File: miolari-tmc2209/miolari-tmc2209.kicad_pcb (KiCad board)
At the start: 2 copper layers, 50 x 49 mm, 32 parts, among them J1 Spread, J2 MS1, J3 MS2, J4 TMC2209_Conn, J5 DriverConn, J9 TMC2209_VIN, U2 TMC2209-LA

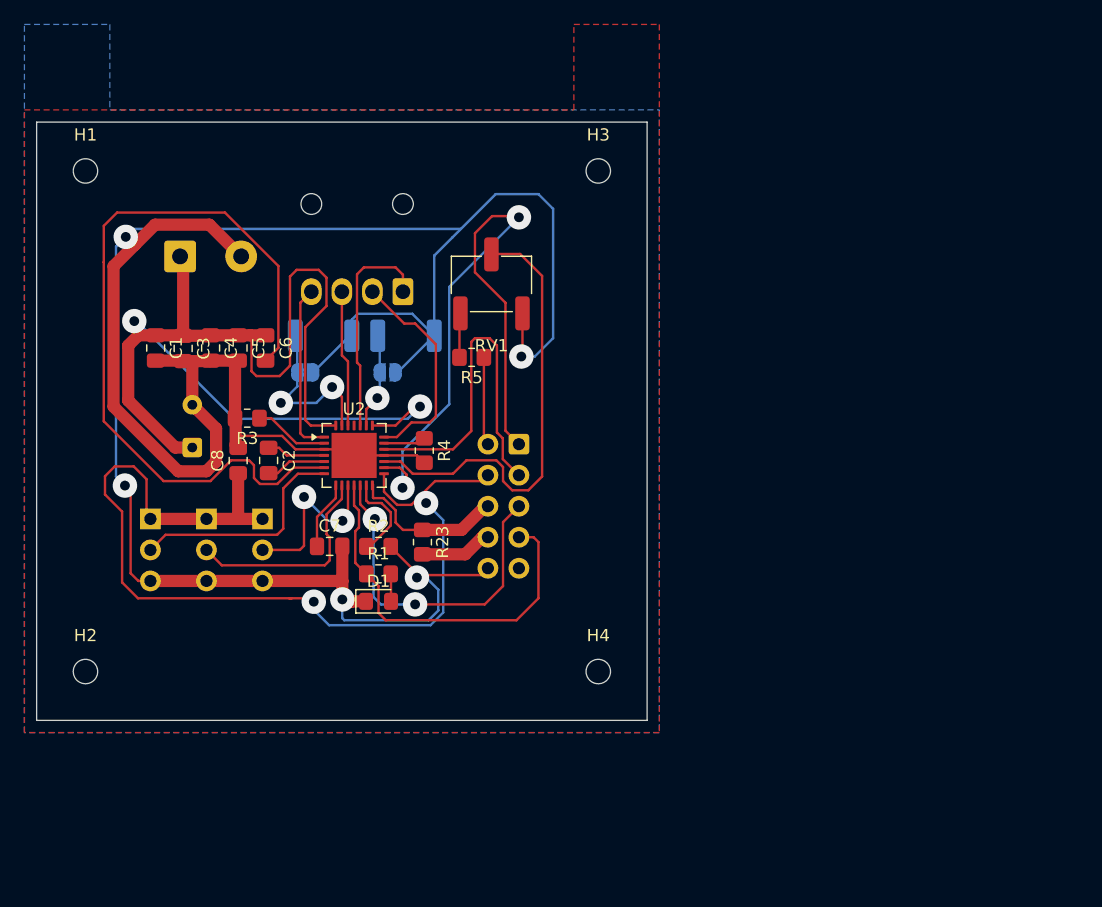
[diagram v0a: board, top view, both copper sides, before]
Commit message: add idc connector to miolari tmc2209
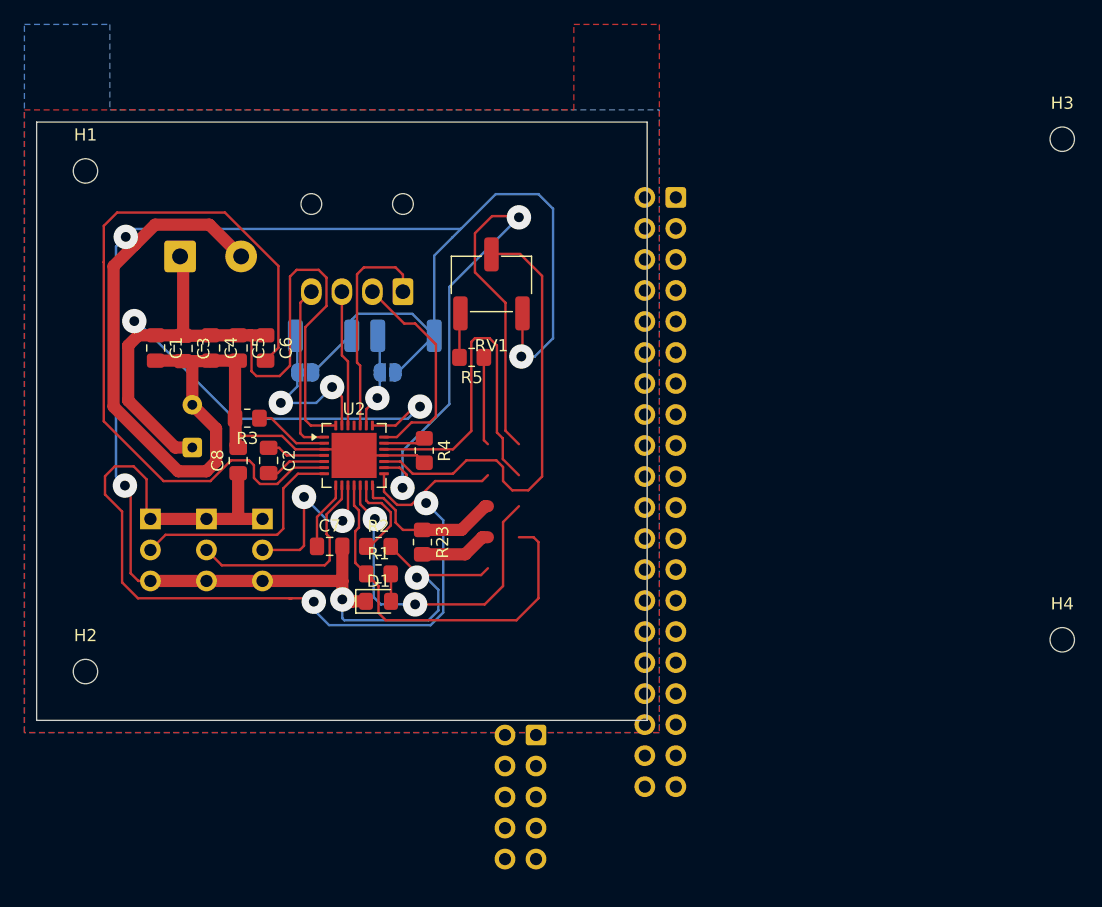
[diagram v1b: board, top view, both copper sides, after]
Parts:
- added J10: MainConnector, Connector_IDC:IDC-Header_2x20_P2.54mm_Vertical, B.Cu at (149.4, 64.2)
- moved H3 38.1 mm to (181.0, 59.4)
- moved H4 38.1 mm to (181.0, 100.4)
- moved J5 23.9 mm to (137.9, 108.2)

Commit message: finish un-tidy miolari tmc2209
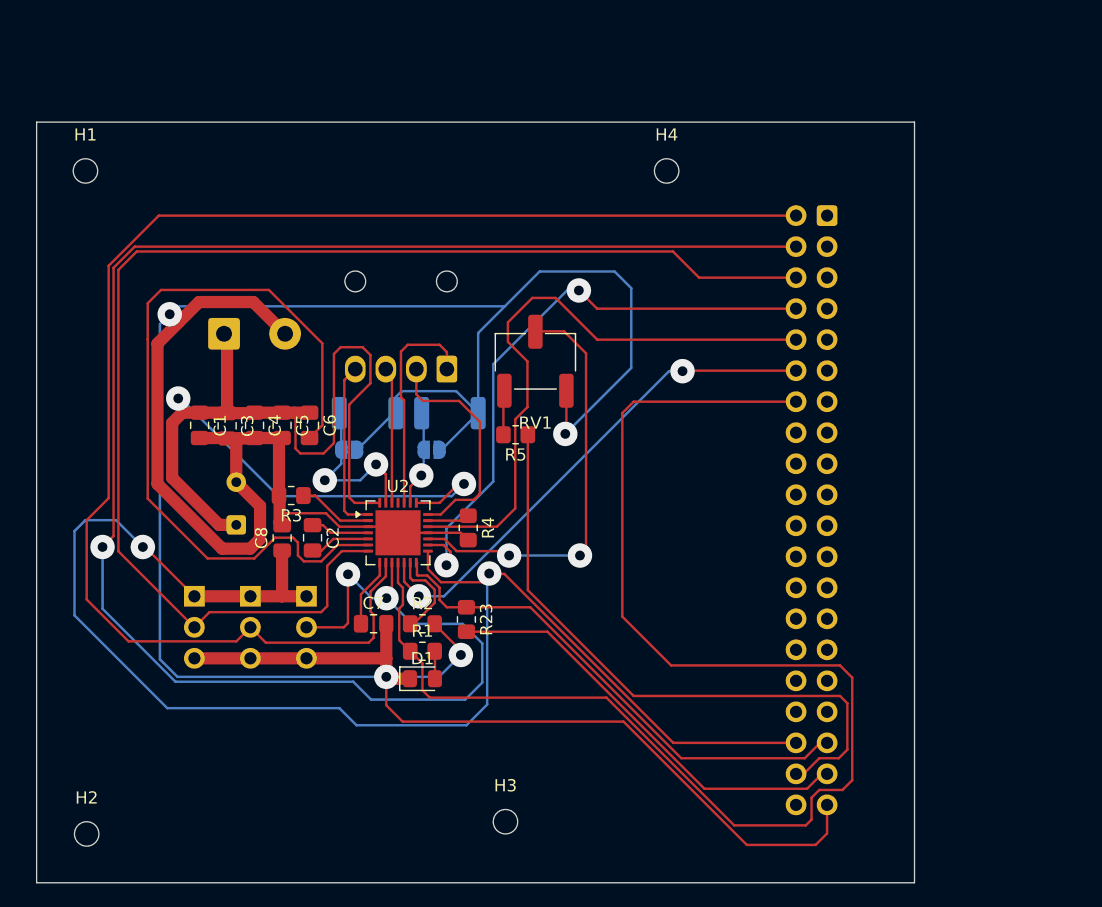
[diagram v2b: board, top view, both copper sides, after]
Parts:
- removed J5: DriverConn, Connector_IDC:IDC-Header_2x05_P2.54mm_Vertical
- moved H3 72.1 mm to (135.4, 115.3)
- moved H4 50.2 mm to (148.6, 62.0)
- moved H2 13.3 mm to (101.1, 116.3)
- moved J10 12.5 mm to (161.7, 65.7)
- moved J1 7.29 mm to (109.9, 96.8)
- moved J2 7.29 mm to (114.5, 96.8)
- moved C1 7.29 mm to (110.3, 82.8)
- moved C3 7.29 mm to (112.6, 82.9)
- moved C4 7.29 mm to (114.8, 82.8)
- moved C5 7.29 mm to (117.1, 82.8)
- moved C6 7.29 mm to (119.3, 82.8)
- moved C7 7.29 mm to (124.6, 99.1)
- moved C8 7.29 mm to (117.1, 92.1)
- moved D1 7.29 mm to (128.6, 103.6)
- moved J3 7.29 mm to (119.1, 96.8)
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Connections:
- J10 pad 38: VBUS -> +5V
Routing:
- net /MS2/AD1: track 14.6 -> 146.9 mm, vias 2 -> 3
- net /MS1/AD0: track 17.5 -> 118.9 mm
- net /SPREAD: track 18.7 -> 107.6 mm
- net /DIAG: track 32.0 -> 114.5 mm
- net GND: track 234.6 -> 288.4 mm, vias 5 -> 4
- net +5V: track 7.25 -> 51.6 mm
- net +3.3V: track 79.6 -> 120.1 mm
- net /UART_TX: track 5.94 -> 35.4 mm
- net /UART_RX: track 13.0 -> 42.1 mm
- net /DIR: track 28.9 -> 49.9 mm
- net /INDEX: track 28.2 -> 41.9 mm
- net /STEP: track 52.4 -> 49.3 mm
- net Net-(U2-VREF): track 37.3 -> 34.7 mm, vias 0 -> 2
- net Net-(J4-Pin_2): track 17.8 -> 19.1 mm
- removed copper zone on B.Cu, net (none)
- removed copper zone on F.Cu, net (none)
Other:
- board size 50 x 49 mm -> 71.9 x 62.3 mm
